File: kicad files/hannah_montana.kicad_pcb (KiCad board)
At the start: 2 copper layers, 59 parts, among them J1 Conn_01x04, SW1 SW_Push, U1 ProMicro

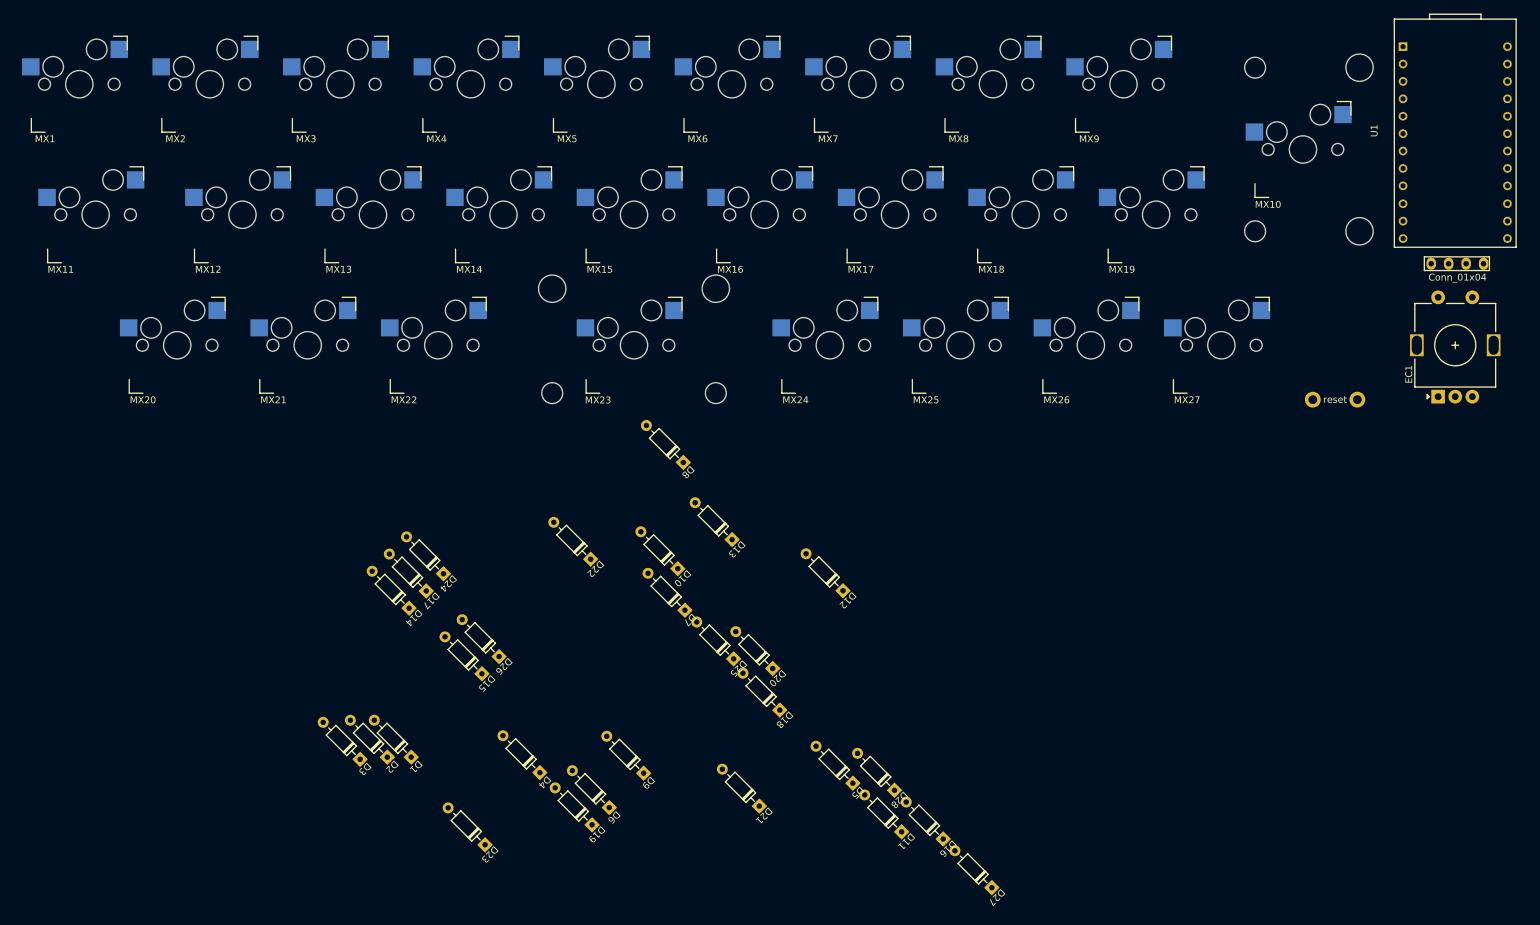
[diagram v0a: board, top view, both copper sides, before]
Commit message: placed pro micro, oled, encoder, rst swtch
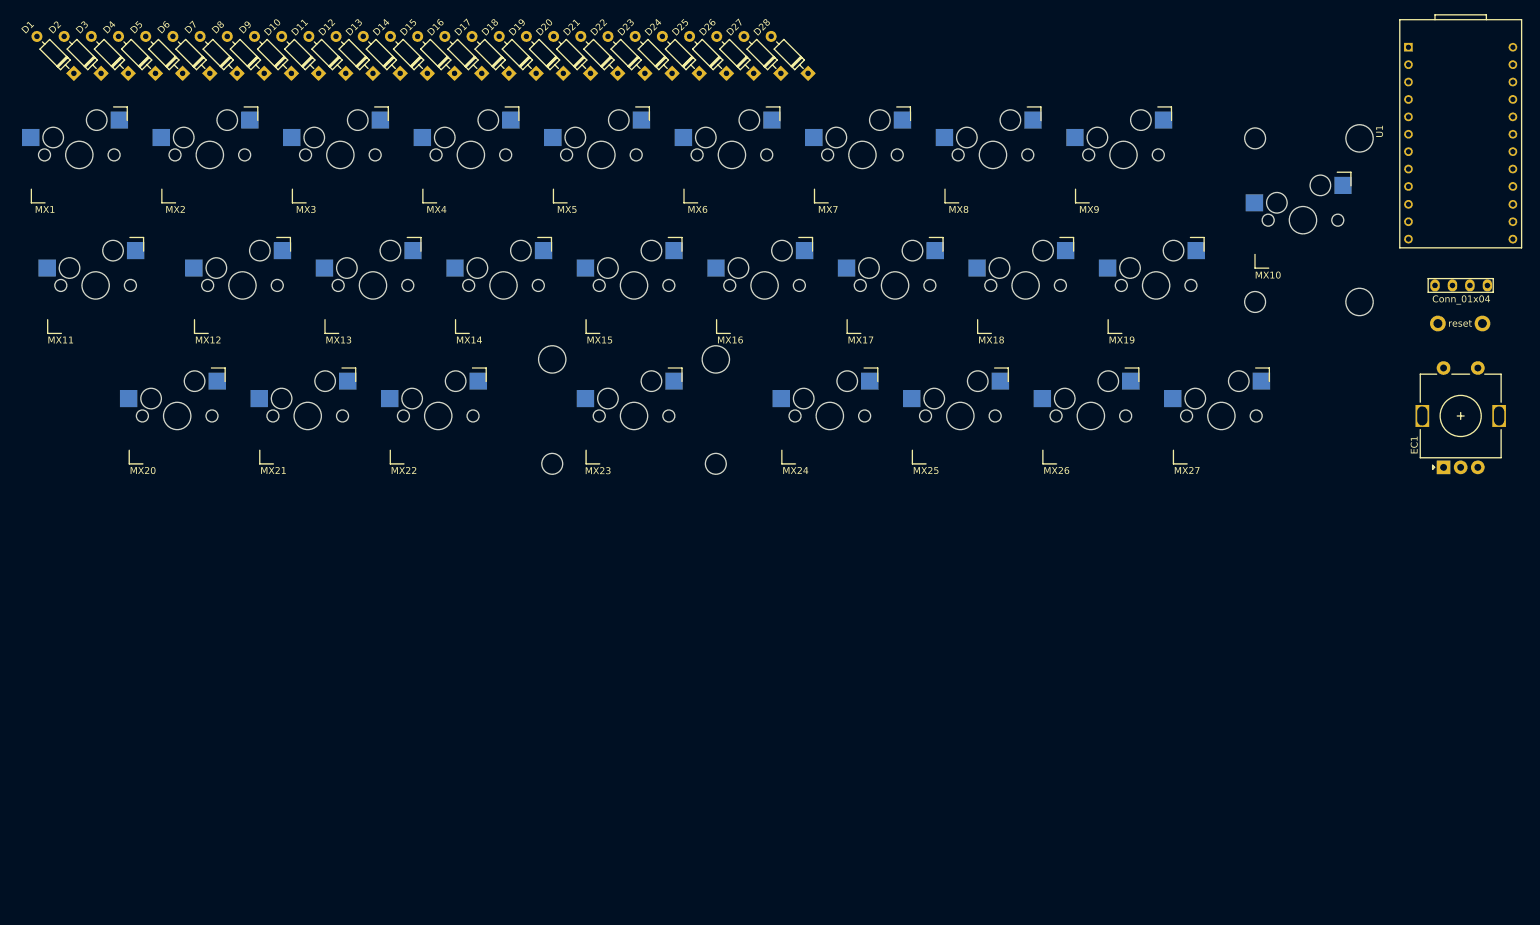
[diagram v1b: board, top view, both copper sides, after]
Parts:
- moved D5 142.5 mm to (24.6, 7.94)
- moved D11 137.2 mm to (48.4, 7.94)
- moved D16 130.5 mm to (68.3, 7.94)
- moved D27 122.8 mm to (111.9, 7.94)
- moved D6 122.0 mm to (28.6, 7.94)
- moved D4 116.5 mm to (20.6, 7.94)
- moved D23 115.9 mm to (96.0, 7.94)
- moved D9 114.4 mm to (40.5, 7.94)
- moved D1 111.3 mm to (8.73, 7.94)
- moved D19 109.8 mm to (80.2, 7.94)
- moved D21 108.9 mm to (88.1, 7.94)
- moved D2 108.2 mm to (12.7, 7.94)
- moved D3 105.7 mm to (16.7, 7.94)
- moved D28 105.4 mm to (115.9, 7.94)
- moved D7 102.0 mm to (32.5, 7.94)
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
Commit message: created pcb outline
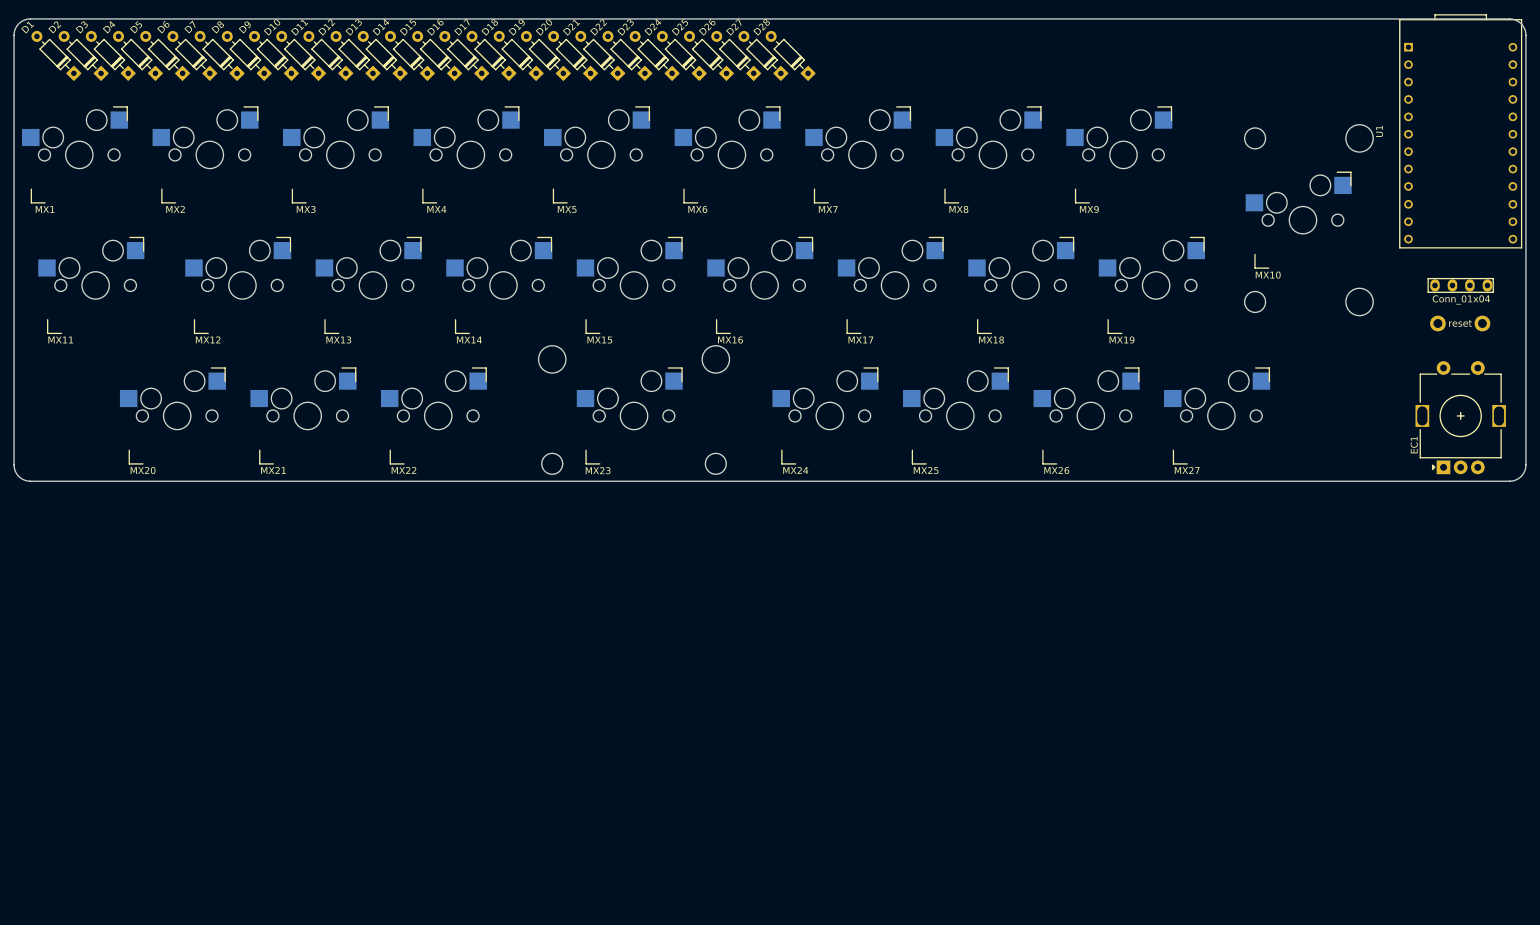
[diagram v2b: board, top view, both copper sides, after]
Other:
- board outline added: 220.7 x 67.5 mm
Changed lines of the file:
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@@
       (net 21 "Net-(D18-Pad2)") (pinfunction "A") (pintype "passive"))
   )
+  (gr_line (start 220.6625 2.38125) (end 220.6625 65.0875) (layer "Edge.Cuts") (width 0.1))
+  (gr_arc (start 2.38125 67.46875) (mid 0.697452 66.771298) (end 0 65.0875) (layer "Edge.Cuts") (width 0.1))
+  (gr_line (start 2.38125 0) (end 218.28125 0) (layer "Edge.Cuts") (width 0.1))
+  (gr_arc (start 220.6625 65.0875) (mid 219.965048 66.771298) (end 218.28125 67.46875) (layer "Edge.Cuts") (width 0.1))
+  (gr_arc (start 218.28125 0) (mid 219.965048 0.697452) (end 220.6625 2.38125) (layer "Edge.Cuts") (width 0.1))
+  (gr_line (start 218.28125 67.46875) (end 2.38125 67.46875) (layer "Edge.Cuts") (width 0.1))
+  (gr_line (start 0 65.0875) (end 0 2.38125) (layer "Edge.Cuts") (width 0.1))
+  (gr_arc (start 0 2.38125) (mid 0.697452 0.697452) (end 2.38125 0) (layer "Edge.Cuts") (width 0.1))
 )

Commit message: routed and rounded everything
i should comit more often. also the routing is terrible i hate it
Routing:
- net col0: track 0.00 -> 324.9 mm, vias 0 -> 8
- net col1: track 0.00 -> 308.5 mm, vias 0 -> 10
- net col4: track 0.00 -> 287.9 mm, vias 0 -> 8
- net col2: track 0.00 -> 284.1 mm, vias 0 -> 10
- net col5: track 0.00 -> 264.9 mm, vias 0 -> 8
- net enccol: track 0.00 -> 262.7 mm, vias 0 -> 10
- net row0: track 0.00 -> 210.6 mm
- net Net-(D10-Pad2): track 0.00 -> 188.8 mm, vias 0 -> 2
- net row1: track 0.00 -> 187.6 mm
- net row2: track 0.00 -> 164.6 mm
- net Net-(D9-Pad2): track 0.00 -> 159.7 mm, vias 0 -> 2
- net Net-(D20-Pad2): track 0.00 -> 155.3 mm, vias 0 -> 2
- net encrow: track 0.00 -> 146.0 mm, vias 0 -> 2
- net Net-(D8-Pad2): track 0.00 -> 144.4 mm, vias 0 -> 2
- net row3: track 0.00 -> 141.7 mm
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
